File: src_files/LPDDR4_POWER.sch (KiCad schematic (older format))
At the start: 58 parts

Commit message: littleupdate
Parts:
- C100, C101, C102, C103, C104, C105, C106, C107, C108, C109, C110, C111, C112, C113, C114, C115, C116, C117, C118, C119, C120, C121, C122, C123, C124, C125, C126, C127, C128, C129, C130, C131, C132, C133, C134, C135, C136, C137, C138, C139, C140, C141, C142, C143, C144, C145, C146, C147, C148, C99: renamed from C?; footprint (none) -> Capacitor_SMD:C_0402_1005Metric
- L10, L11: renamed from L?; footprint (none) -> 74438357068_ind:74438357068
- R25, R26, R27: renamed from R?; footprint (none) -> Resistor_SMD:R_0402_1005Metric
- gave numbers to parts that had none: 3

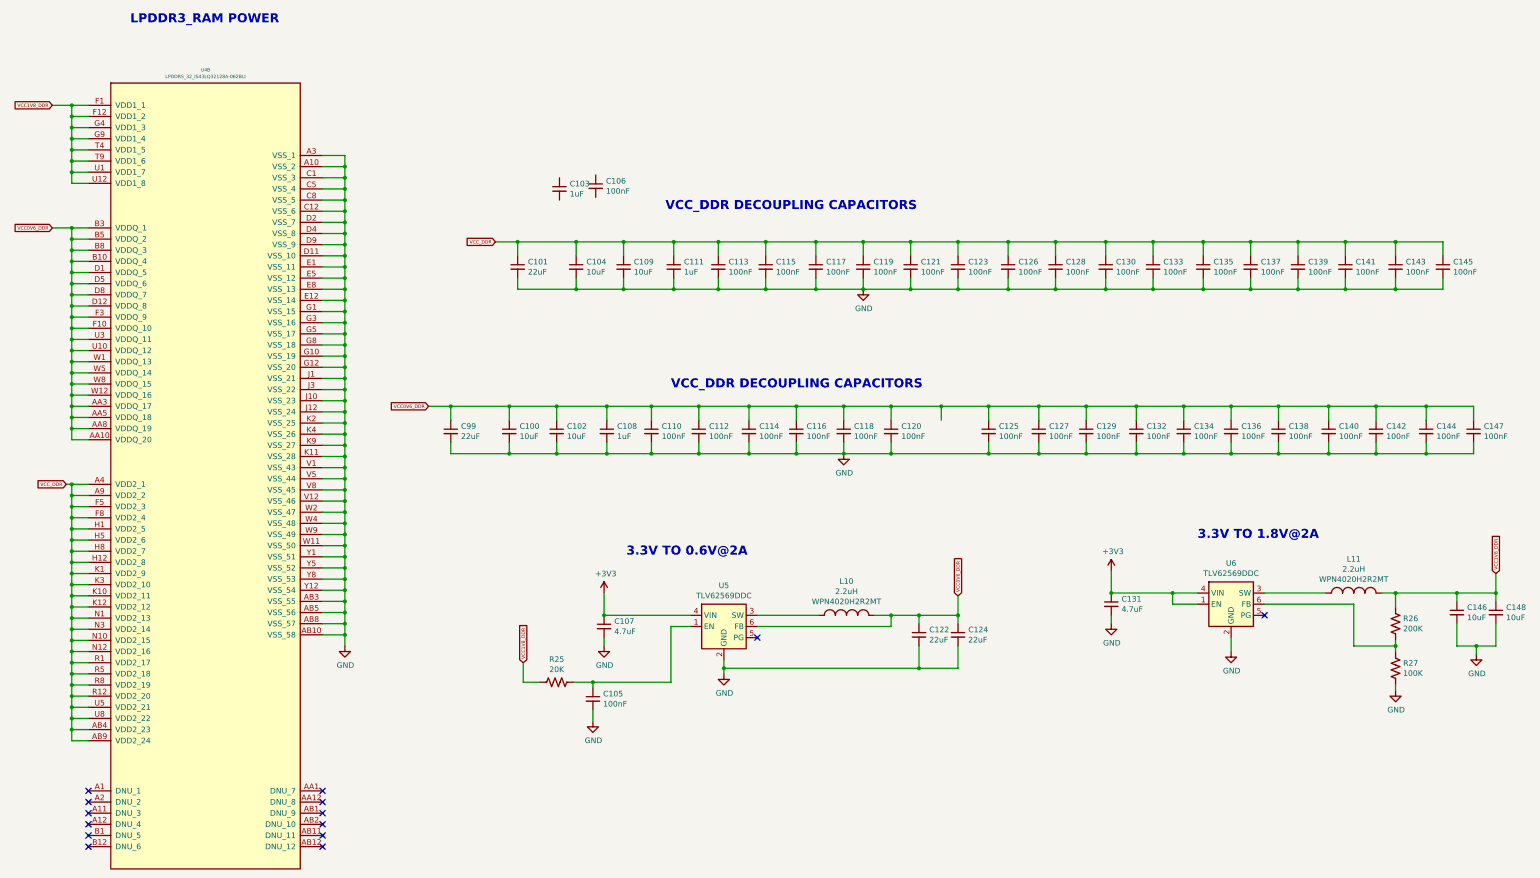
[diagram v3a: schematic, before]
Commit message: schematic capture complete
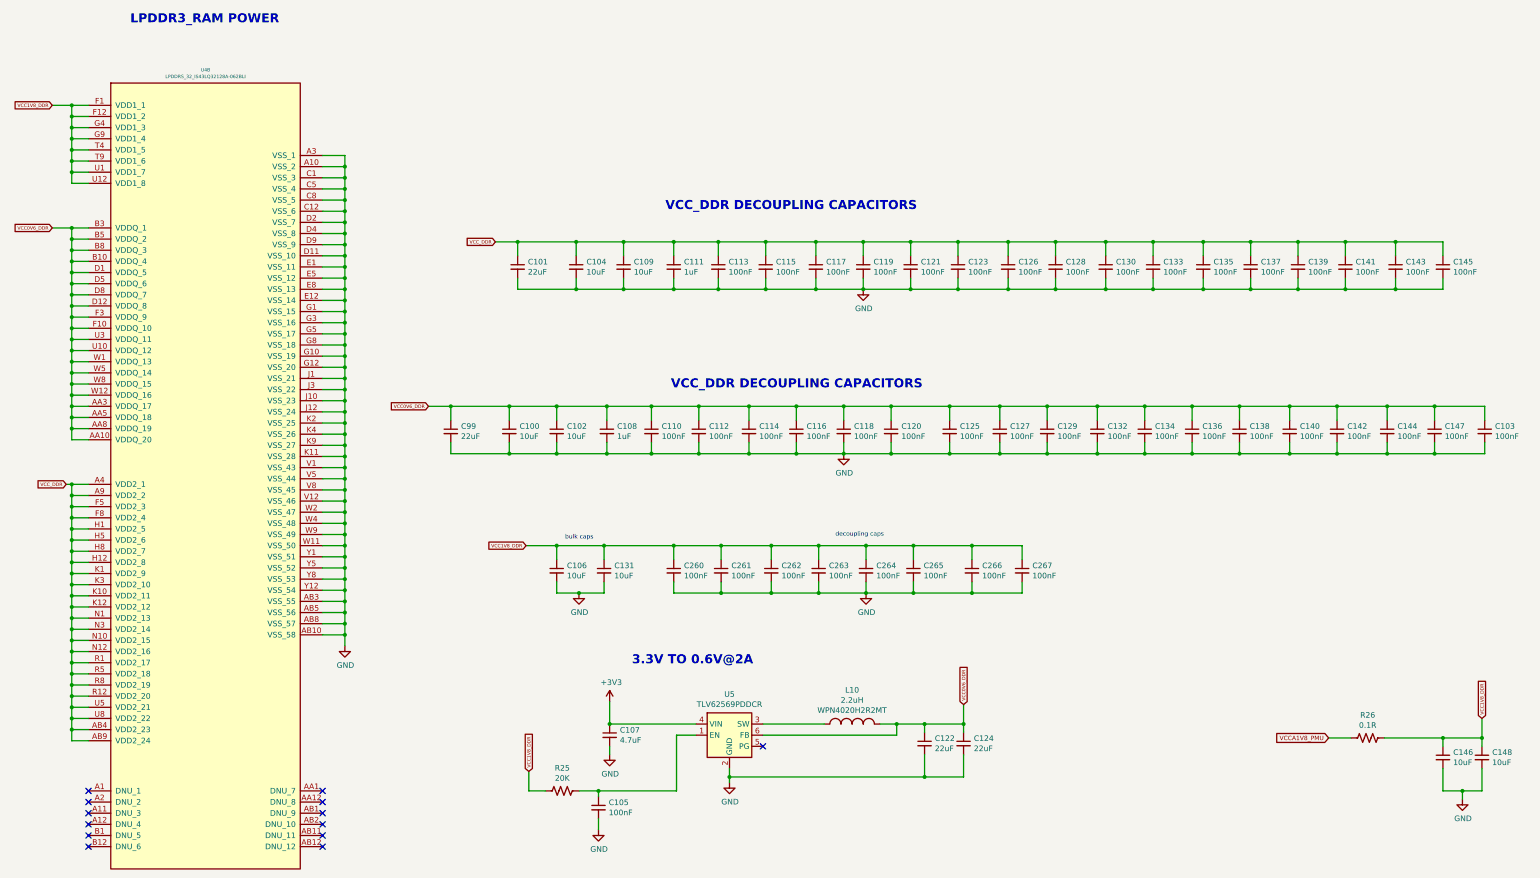
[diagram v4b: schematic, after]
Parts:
- removed L11: 2.2uH, 74438357068_ind:74438357068, symbol OLIMEX_RCL:INDUCTOR_SMALL
- removed R27: 100K, Resistor_SMD:R_0402_1005Metric, symbol Device:R_US
- removed U6: TLV62569DDC, Package_TO_SOT_SMD:SOT-23-6, symbol Regulator_Switching:TLV62569DDC
- added C260, C261, C262, C263, C264, C265, C266, C267: 100nF, Capacitor_SMD:C_0402_1005Metric, symbol Device:C_Small
- C103: value 1uF -> 100nF
- C106: value 100nF -> 10uF
- C131: value 4.7uF -> 10uF
- L10: footprint 74438357068_ind:74438357068 -> greencharge-footprints:WPN4020H2R2MT
- R26: value 200K -> 0.1R
- U5: value TLV62569DDC -> TLV62569PDDCR
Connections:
- net +3V3: no longer C131.1
- net GND: now also C103.2, C106.2, C260.2, C261.2, C262.2, C263.2, C264.2, C265.2, C266.2, C267.2
- net VCC0V6_DDR: now also C103.1
- net VCC1V8_DDR: now also C106.1, C131.1, C260.1, C261.1, C262.1, C263.1, C264.1, C265.1, C266.1, C267.1
- net VCCA1V8_PMU: now reaches R26.2
- no-connect marks 14 -> 13
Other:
- note added: "bulk caps\n"
- note added: "decoupling caps"
- note removed: "3.3V TO 1.8V@2A\n"
- moved on the sheet: C105, C107, C122, C124, C125, C127, C129, C132, C134, C136, C138, C140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

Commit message: updated footprint and schematics
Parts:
- U4: value LPDDRS_32_IS43LQ32128A-062BLI -> LPDDR4_32_IS43LQ32128A-062BLI
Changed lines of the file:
@@
 $Descr A3 16535 11693
 encoding utf-8
-Sheet 9 15
+Sheet 9 16
 Title ""
 Date ""
@@
 P 4250 1900
 F 0 "U4" H 4150 1918 30  0000 C CNN
-F 1 "LPDDRS_32_IS43LQ32128A-062BLI" H 4150 1858 30  0000 C CNN
+F 1 "LPDDR4_32_IS43LQ32128A-062BLI" H 4150 1858 30  0000 C CNN
 F 2 "greencharge-footprints:BGA200C65P12X22_1000X1450X85" H 3800 1600 30  0001 C CNN
 F 3 "" H 3800 1600 30  0001 C CNN
